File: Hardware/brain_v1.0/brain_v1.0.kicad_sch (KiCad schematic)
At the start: 0 parts

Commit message: almost finished design of power board and working through design of brain board
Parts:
- added C1: 0.1uF, symbol device:C_Small
- added C2, C3: 1uF, symbol device:C_Small
- added D4, D5: D_Schottky, symbol device:D_Schottky
- added J2, J3, J4, J6: Conn_01x02, symbol Connector_Generic:Conn_01x02
- added JP1: SolderJumper_3_Open, symbol Jumper:SolderJumper_3_Open
- added Q1, Q2, Q3, Q4: BSS138, Package_TO_SOT_SMD:SOT-23, symbol Transistor_FET:BSS138
- added Q5, Q6: SMD-TRANSISTORS-NPN-25V-500MW_SOT-23_, SMD-TRANSISTORS-NPN-25V-500MW_SOT-23_:SOT-23, symbol S8050-SMD:SMD-TRANSISTORS-NPN-25V-500MW_SOT-23_
- added R1, R3: 100k, symbol device:R_US
- added R10, R11, R12, R13, R14, R15, R2, R30, R6, R7, R8, R9: 10k, symbol device:R_US
- added SW1, SW3: SW_Push, symbol Switch:SW_Push
- added TP1, TP2, TP3, TP4: TestPoint, symbol Connector:TestPoint
- added U1: ESP32-WROOM-32E 4MB, symbol ESP32-WROOM-32E-N4:ESP32-WROOM-32E_4MB
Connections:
- new net: J6.2 (Pin_2), Q4.3 (D), R13.2, TP4.1
- new net: J2.2 (Pin_2), Q1.3 (D), R8.2, TP1.1
- new net: Q5.1, R7.2
- new net: Q5.3, R2.1
- new net: J4.2 (Pin_2), Q3.3 (D), R12.2, TP3.1
- new net: J3.2 (Pin_2), Q2.3 (D), R10.2, TP2.1
- new net: D4.1 (K), JP1.1 (A)
- new net: JP1.2 (C), U1.2 (3V3)
- new net: D5.1 (K), JP1.3 (B)
- new net: Q6.1, R30.2
- new net: Q6.3, R6.1
- new net +3V3: C1.1, D4.2 (A), Q1.1 (G), Q2.1 (G), Q3.1 (G), Q4.1 (G), R1.1, R11.1, R14.1, R15.1, R3.1, R9.1
- new net +5V: R10.1, R12.1, R13.1, R8.1
- new net 3v3_backup: D5.2 (A)
- new net CHIP_PU: C3.1, R2.2, R3.2, SW3.2, U1.3 (EN)
- new net DTR: Q6.2, R7.1
- new net GND: C1.2, C2.2, C3.2, J2.1 (Pin_1), J3.1 (Pin_1), J4.1 (Pin_1), J6.1 (Pin_1), SW1.1, SW3.1, U1.1 (GND), U1.15 (GND), U1.38 (GND), U1.39 (GND), U1.40 (GND), U1.41 (GND), U1.42 (GND), U1.43 (GND), U1.44 (GND), U1.45 (GND), U1.46 (GND), U1.47 (GND)
- new net GPIO0_STRAPPING: C2.1, R1.2, R6.2, SW1.2, U1.25 (IO0)
- new net Load_Cell_1: Q1.2 (S), R9.2
- new net Load_Cell_2: Q2.2 (S), R11.2
- new net RFID_MISO: U1.31 (IO19)
- new net RFID_MOSI: U1.37 (IO23)
- new net RFID_RST: U1.36 (IO22)
- new net RFID_SCK: U1.30 (IO18)
- new net RFID_SDA: U1.29 (IO5)
- new net RTS: Q5.2, R30.1
- new net RX: U1.34 (RXD0)
- new net Sensor1: Q3.2 (S), R14.2
- new net Sensor2: Q4.2 (S), R15.2
- new net TX: U1.35 (TXD0)
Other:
- added sheet Power Subcircuits (Power.kicad_sch)
- note added: "Level Shifters"
- company: (none) -> ECE 445: Senior Capstone Project
- title: Template -> Brain Board

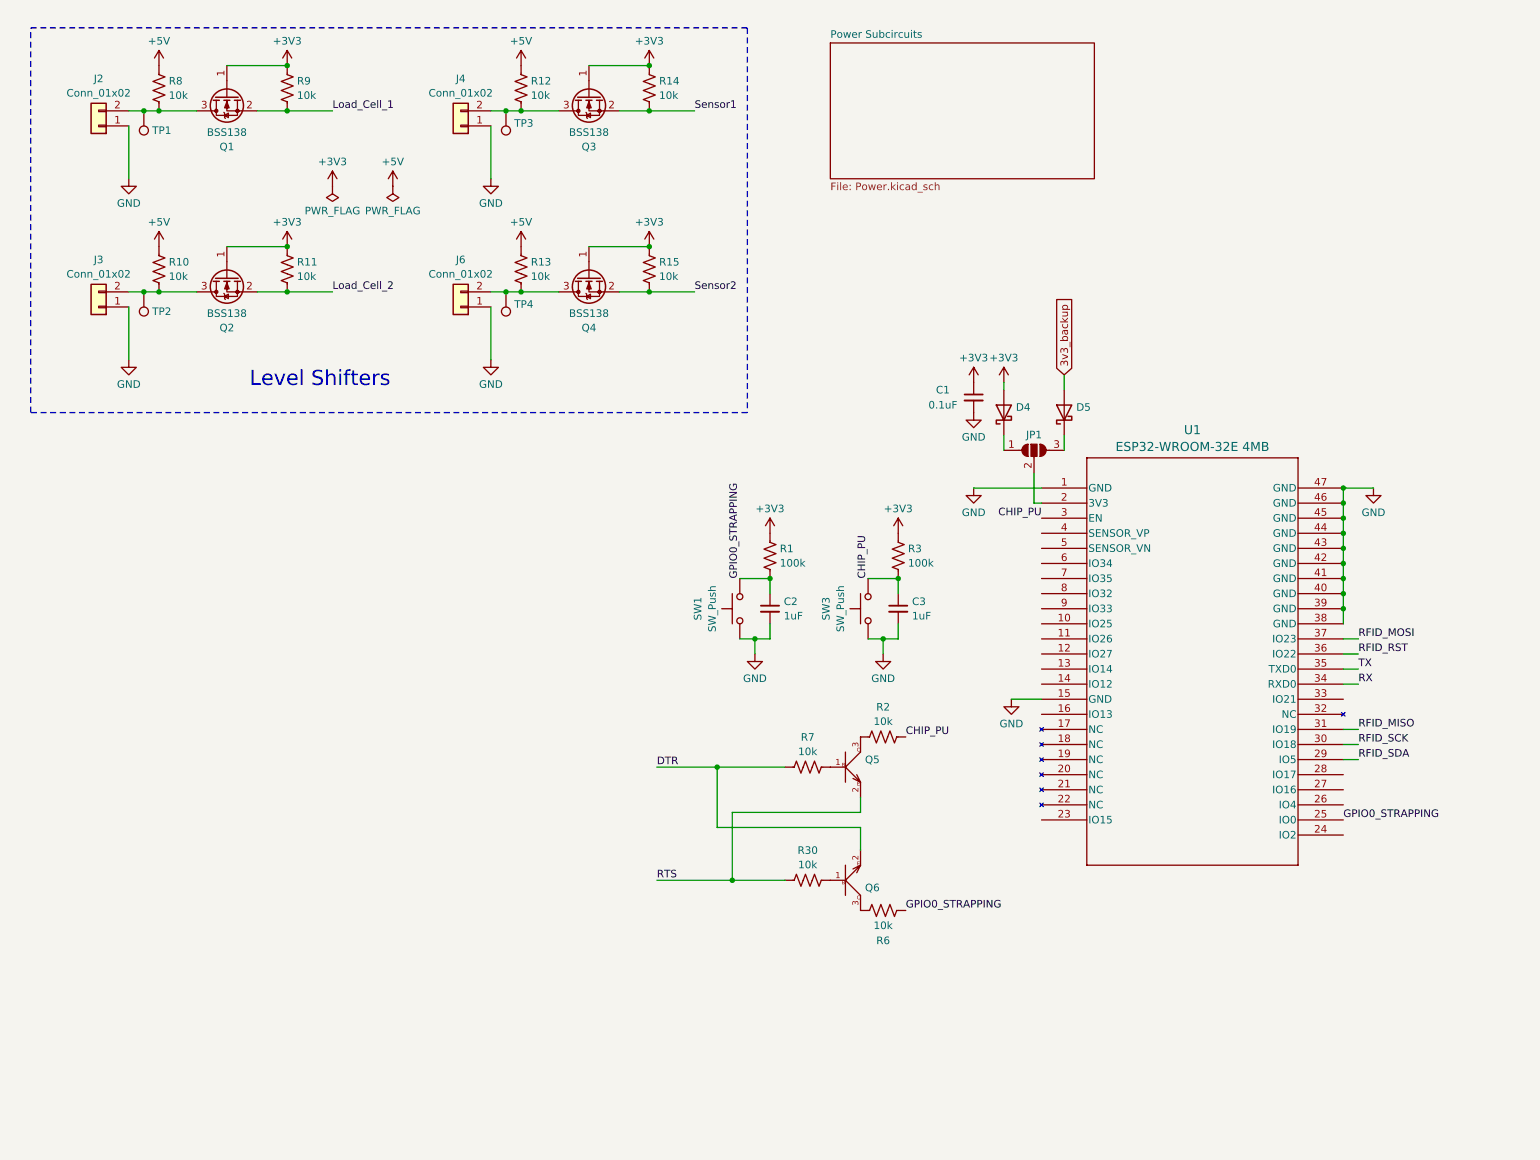
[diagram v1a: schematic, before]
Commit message: brain design pretty much done if RFID not needed
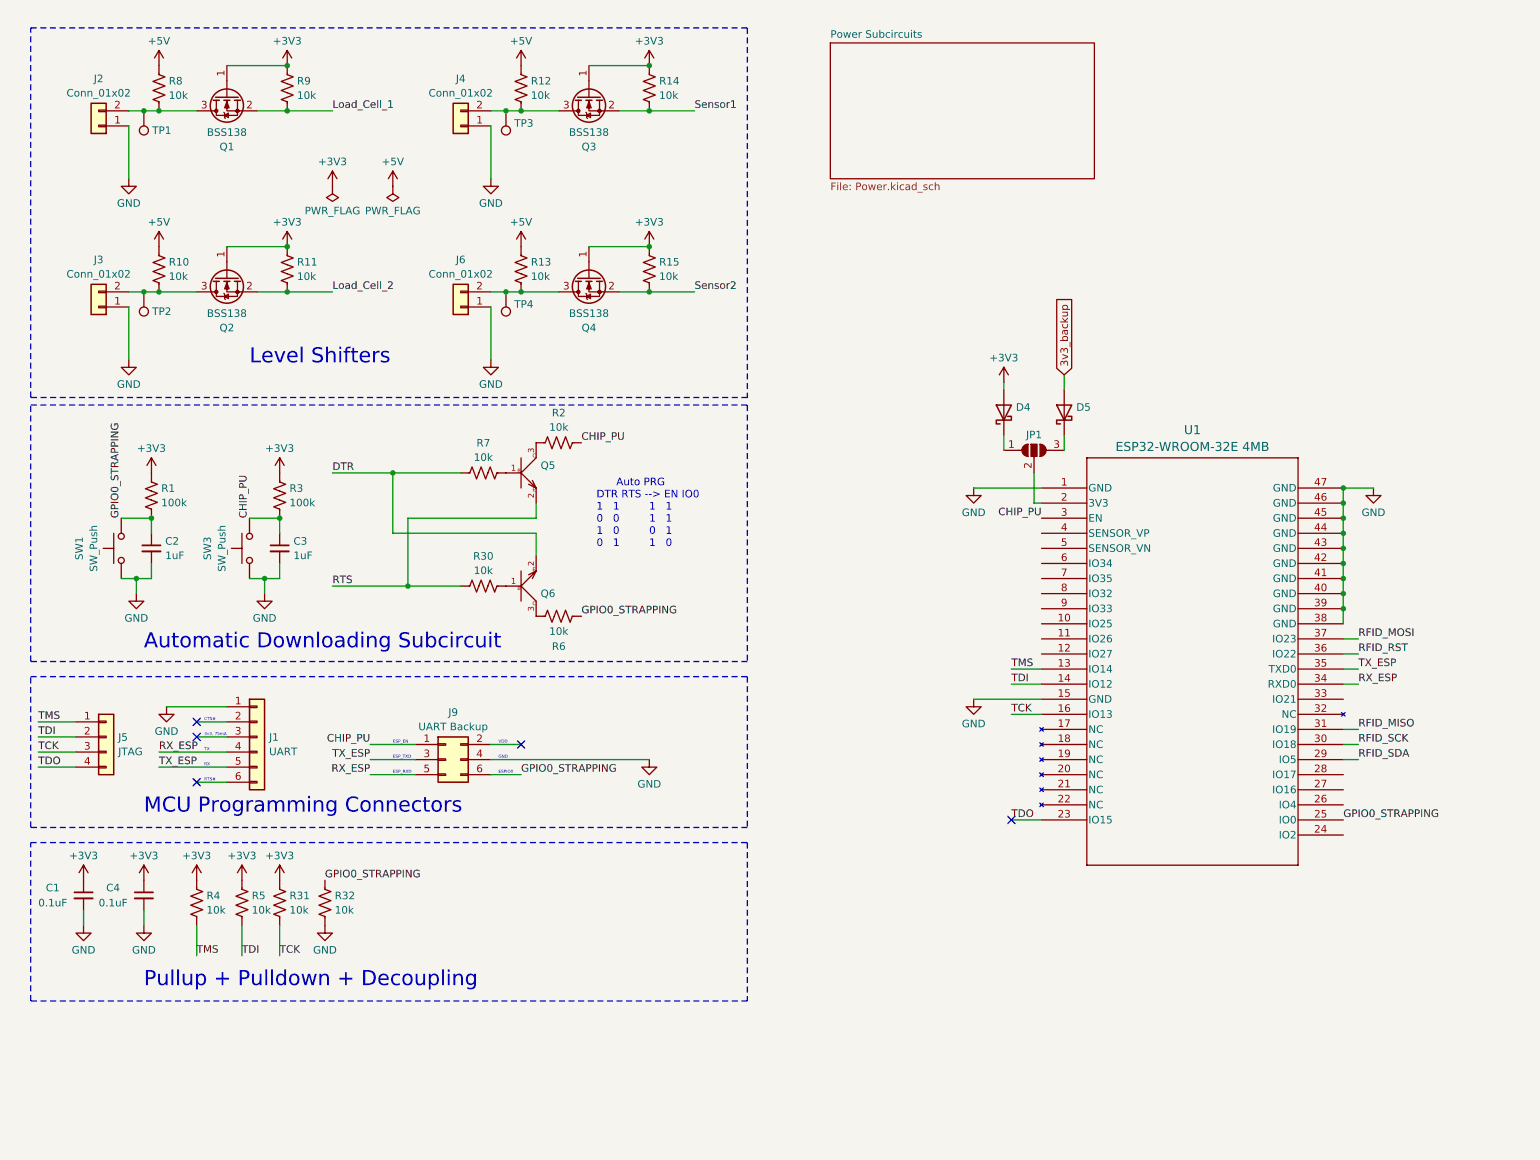
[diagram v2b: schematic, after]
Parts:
- added C4: 0.1uF, symbol device:C_Small
- added J1: UART, symbol Connector_Generic:Conn_01x06
- added J5: JTAG, symbol Connector_Generic:Conn_01x04
- added J9: UART Backup, symbol Connector_Generic:Conn_02x03_Odd_Even
- added R31, R32, R4, R5: 10k, symbol Device:R_US
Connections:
- net +3V3: now also C4.1, R31.1, R4.1, R5.1
- net CHIP_PU: now also J9.1 (Pin_1)
- net GND: now also C4.2, J1.1 (Pin_1), J9.4 (Pin_4), R32.2
- net GPIO0_STRAPPING: now also J9.6 (Pin_6), R32.1
- net TMS: now reaches U1.13 (IO14)
- net TMS: now also J5.1 (Pin_1), R4.2
- net TDI: now reaches U1.14 (IO12)
- net TDI: now also J5.2 (Pin_2), R5.2
- net TCK: now reaches U1.16 (IO13)
- net TCK: now also J5.3 (Pin_3), R31.2
- net TDO: now reaches U1.23 (IO15)
- net TDO: now also J5.4 (Pin_4)
- net RX renamed RX_ESP
- net RX_ESP: now also J1.4 (Pin_4), J9.5 (Pin_5)
- net TX renamed TX_ESP
- net TX_ESP: now also J1.5 (Pin_5), J9.3 (Pin_3)
- no-connect marks 0 -> 5
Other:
- note added: "3v3, 75mA"
- note added: "Auto PRG DTR RTS --> EN IO0 1 1 1 1 0 0 1 1 1 0 0 1 0 1 1 0"
- note added: "Automatic Downloading Subcircuit"
- note added: "CTS#"
- note added: "ESPIO0"
- note added: "ESP_EN"
- note added: "ESP_RXD"
- note added: "ESP_TXD"
- note added: "GND"
- note added: "MCU Programming Connectors"
- note added: "Pullup + Pulldown + Decoupling"
- note added: "RTS#"
- note added: "RX"
- note added: "TX"
- note added: "VDD"
- moved on the sheet: C1, C2, C3, Q5, Q6, R1, R2, R3, R30, R6, R7, SW1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

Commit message: finished part selection for power and almost done with part selection for brain--moving to layout next
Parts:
- added H1, H2, H3, H4: MountingHole, MountingHole:MountingHole_3.2mm_M3, symbol Mechanical:MountingHole
- added R33: 10k, Resistor_SMD:R_1206_3216Metric, symbol Device:R_US
- C1, C4: footprint (none) -> Capacitor_SMD:C_0603_1608Metric; Link (none) -> https://www.digikey.com/en/products/detail/kemet/C0603C103F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; MPN (none) -> C0603C103F3GECAUTO
- C2, C3: footprint (none) -> Resistor_SMD:R_0603_1608Metric; Link (none) -> https://www.digikey.com/en/products/detail/taiyo-yuden/TMK1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; MPN (none) -> TMK107B7105KA-T
- D4, D5: footprint (none) -> VS_30BQ015_M3_9AT:VS_30BQ015_M3_9AT; Link (none) -> https://www.digikey.com/en/products/detail/vishay-general-s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; MPN (none) -> VS-30BQ015-M3/9AT
- J2, J3, J4, J6: footprint (none) -> Connector_Molex:Molex_KK-254_AE-6410-02A_1x02_P2.54mm_Vertical; Link (none) -> https://www.digikey.com/en/products/detail/molex/1718560102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; MPN (none) -> 1718560102
- JP1: footprint (none) -> Jumper:SolderJumper-3_P1.3mm_Open_RoundedPad1.0x1.5mm; Link (none) -> NA; MPN (none) -> NA
- Q1, Q2, Q3, Q4: Link (none) -> https://www.digikey.com/en/products/detail/onsemi/BSS138/24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; MPN (none) -> BSS138
- Q5, Q6: Link (none) -> https://www.digikey.com/en/products/detail/nextgen-componen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
- R1, R3: footprint (none) -> Resistor_SMD:R_0805_2012Metric; Link (none) -> https://www.digikey.com/en/products/detail/yageo/RC0805FR-0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; MPN (none) -> RC0805FR-07100KL
- R10, R11, R12, R13, R14, R15, R2, R30, R31, R32, R4, R5, R6, R7, R8, R9: footprint (none) -> Resistor_SMD:R_1206_3216Metric; Link (none) -> https://www.digikey.com/en/products/detail/susumu/HRG3216P-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; MPN (none) -> HRG3216P-1002-B-T1
- SW1, SW3: footprint (none) -> Button_Switch_SMD:SW_SPST_B3U-1000P; Link (none) -> https://www.digikey.com/en/products/detail/omron-electronic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; MPN (none) -> B3U-1000P
- TP1, TP2, TP3, TP4: footprint (none) -> TestPoint:TestPoint_Keystone_5010-5014_Multipurpose; Link (none) -> https://www.digikey.com/en/products/detail/keystone-electro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; MPN (none) -> 36-5011-ND
- U1: footprint (none) -> ESP32-WROOM-32E-N4:ESP32-WROOM-32E-N4; Link (none) -> https://www.digikey.com/en/products/detail/espressif-system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; MPN (none) -> ESP32-WROOM-32E-N4
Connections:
- net GND: now also R33.2
- net GPIO2: now reaches U1.24 (IO2)
- net GPIO2: now also R33.1
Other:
- note added: "MCU Pullup + Pulldown + Decoupling"
- note removed: "Pullup + Pulldown + Decoupling"
